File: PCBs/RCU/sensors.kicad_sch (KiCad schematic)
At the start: 8 parts, among them U500 APDS-9306-065, U501 LSM6DS3, U502 SHT30-DIS

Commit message: Schematic cleanup
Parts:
- C504: value 0.1u -> (none)
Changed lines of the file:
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@@
       (effects (font (size 1.27 1.27)) (justify left))
     )
-    (property "Value" "0.1u" (id 1) (at 21.59 113.0299 0)
+    (property "Value" "" (id 1) (at 21.59 113.0299 0)
       (effects (font (size 1.27 1.27)) (justify left))
     )

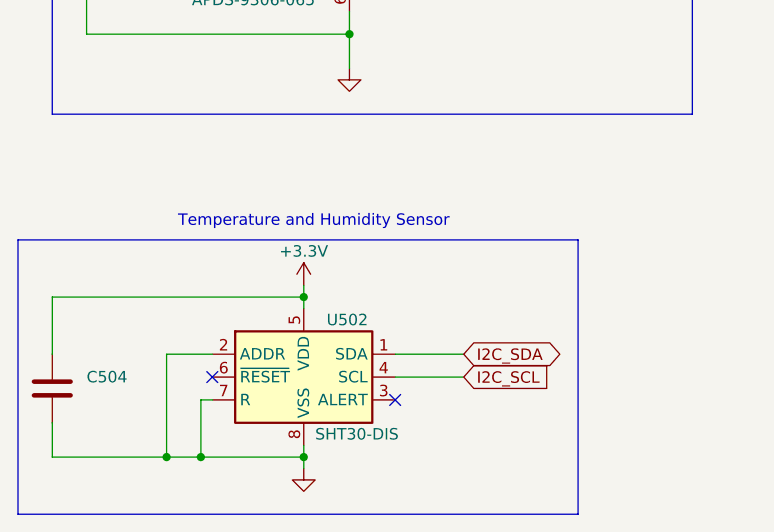
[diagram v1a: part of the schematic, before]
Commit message: Wrote that first regulator in power schematic also powers the external memory
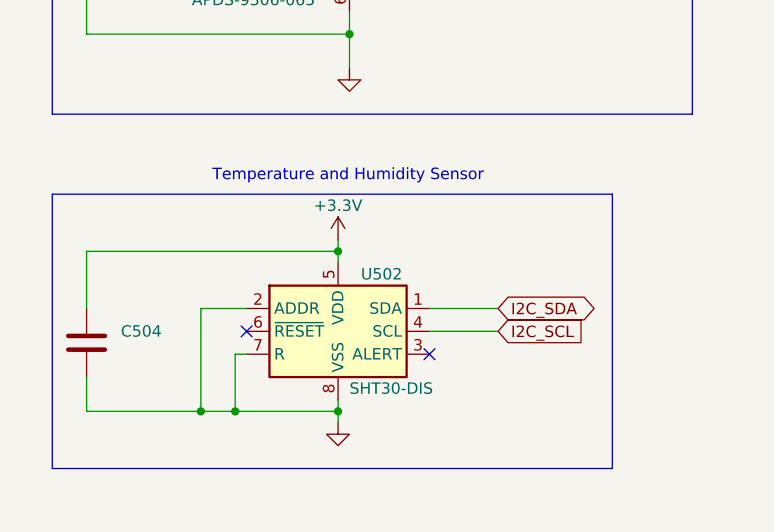
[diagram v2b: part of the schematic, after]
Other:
- moved on the sheet: C504, U502

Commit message: Corrected SPI_MOSI and SPI_MISO labels on U700 - external memory
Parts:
- C504: value (none) -> 0.1uF
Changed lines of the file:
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@@
       (effects (font (size 1.27 1.27)) (justify left))
     )
-    (property "Value" "" (id 1) (at 25.4 107.9499 0)
+    (property "Value" "0.1uF" (id 1) (at 25.4 107.9499 0)
       (effects (font (size 1.27 1.27)) (justify left))
     )

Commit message: Change address pin of left motor ADC to floating so that it and the light sensor will have diffeent addresses, wrote slave addresses for ADCs and light sensor
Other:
- note added: "Slave Address: 1010010"
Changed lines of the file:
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@@
+    (effects (font (size 1.27 1.27)) (justify left bottom))
+  )
+  (text "Slave Address: 1010010" (at 55.88 69.85 0)
     (effects (font (size 1.27 1.27)) (justify left bottom))
   )

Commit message: Wrote slave address for all I2C ICs in binary and hex
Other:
- note added: "Slave Address: 1000100 - 0x44"
- note added: "Slave Address: 1010010 - 0x52"
- note added: "Slave Address: 1101010 - 0x6A"
- note removed: "Slave Address: 1010010"
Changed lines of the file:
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@@
     (stroke (width 0) (type default) (color 0 0 0 0))
   )
-  (polyline (pts (xy 80.01 120.65) (xy 17.78 120.65))
+  (polyline (pts (xy 85.09 120.65) (xy 17.78 120.65))
     (stroke (width 0) (type default) (color 0 0 0 0))
   )
@@
     (stroke (width 0) (type default) (color 0 0 0 0))
   )
-  (polyline (pts (xy 80.01 90.17) (xy 80.01 120.65))
+  (polyline (pts (xy 85.09 90.17) (xy 85.09 120.65))
     (stroke (width 0) (type default) (color 0 0 0 0))
   )
@@
     (stroke (width 0) (type default) (color 0 0 0 0))
   )
-  (polyline (pts (xy 17.78 90.17) (xy 80.01 90.17))
+  (polyline (pts (xy 17.78 90.17) (xy 85.09 90.17))
     (stroke (width 0) (type default) (color 0 0 0 0))
+  )
+  (text "Slave Address: 1101010 - 0x6A" (at 154.94 86.36 0)
+    (effects (font (size 1.27 1.27)) (justify left bottom))
   )
   (text "Temperature and Humidity Sensor" (at 35.56 88.9 0)
@@
     (effects (font (size 5.08 5.08) (thickness 1.016) bold italic) (justify left bottom))
   )
+  (text "Slave Address: 1000100 - 0x44" (at 52.07 115.57 0)
+    (effects (font (size 1.27 1.27)) (justify left bottom))
+  )
   (text "Accelerometer & Gyroscope" (at 129.54 36.83 0)
     (effects (font (size 1.27 1.27)) (justify left bottom))
@@
     (effects (font (size 1.27 1.27)) (justify left bottom))
   )
-  (text "Slave Address: 1010010" (at 55.88 69.85 0)
+  (text "Slave Address: 1010010 - 0x52" (at 55.88 69.85 0)
     (effects (font (size 1.27 1.27)) (justify left bottom))
   )

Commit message: Add footrpints to TVS diodes in [3]
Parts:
- C500: value 1uF -> (none)
- C501, C502, C504: value 0.1uF -> (none)
- R500: value 10k -> (none)
- U500: value APDS-9306-065 -> (none); footprint OptoDevice:Broadcom_DFN-6_2x2mm_P0.65mm -> (none)
- U501: value LSM6DS3 -> (none); footprint Package_LGA:LGA-14_3x2.5mm_P0.5mm_LayoutBorder3x4y -> (none)
- U502: value SHT30-DIS -> (none); footprint Sensor_Humidity:Sensirion_DFN-8-1EP_2.5x2.5mm_P0.5mm_EP1.1x1.7mm -> (none)
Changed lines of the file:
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@@
   (symbol (lib_id "power:GND") (at 120.65 62.23 0) (unit 1)
     (in_bom yes) (on_board yes) (fields_autoplaced)
-    (property "Reference" "#PWR?" (id 0) (at 120.65 68.58 0)
+    (property "Reference" "#PWR0178" (id 0) (at 120.65 68.58 0)
       (effects (font (size 1.27 1.27)) hide)
     )
@@
   (symbol (lib_id "power:GND") (at 161.29 67.31 0) (unit 1)
     (in_bom yes) (on_board yes) (fields_autoplaced)
-    (property "Reference" "#PWR?" (id 0) (at 161.29 73.66 0)
+    (property "Reference" "#PWR0184" (id 0) (at 161.29 73.66 0)
       (effects (font (size 1.27 1.27)) hide)
     )
@@
       (effects (font (size 1.27 1.27)) (justify left))
     )
-    (property "Value" "1uF" (id 1) (at 25.4 63.4999 0)
+    (property "Value" "" (id 1) (at 25.4 63.4999 0)
       (effects (font (size 1.27 1.27)) (justify left))
     )
@@
   (symbol (lib_id "power:GND") (at 50.8 76.2 0) (unit 1)
     (in_bom yes) (on_board yes) (fields_autoplaced)
-    (property "Reference" "#PWR?" (id 0) (at 50.8 82.55 0)
+    (property "Reference" "#PWR0182" (id 0) (at 50.8 82.55 0)
       (effects (font (size 1.27 1.27)) hide)
     )
@@
   (symbol (lib_id "power:+3.3V") (at 50.8 50.8 0) (unit 1)
     (in_bom yes) (on_board yes)
-    (property "Reference" "#PWR?" (id 0) (at 50.8 54.61 0)
+    (property "Reference" "#PWR0181" (id 0) (at 50.8 54.61 0)
       (effects (font (size 1.27 1.27)) hide)
     )
@@
   (symbol (lib_id "power:+3.3V") (at 119.38 92.71 0) (unit 1)
     (in_bom yes) (on_board yes)
-    (property "Reference" "#PWR?" (id 0) (at 119.38 96.52 0)
+    (property "Reference" "#PWR0179" (id 0) (at 119.38 96.52 0)
       (effects (font (size 1.27 1.27)) hide)
     )
@@
       (effects (font (size 1.27 1.27)) (justify left))
     )
-    (property "Value" "SHT30-DIS" (id 1) (at 50.8 111.76 0)
-      (effects (font (size 1.27 1.27)) (justify left))
-    )
-    (property "Footprint" "Sensor_Humidity:Sensirion_DFN-8-1EP_2.5x2.5mm_P0.5mm_EP1.1x1.7mm" (id 2) (at 49.53 104.14 0)
+    (property "Value" "" (id 1) (at 50.8 111.76 0)
+      (effects (font (size 1.27 1.27)) (justify left))
+    )
+    (property "Footprint" "" (id 2) (at 49.53 104.14 0)
       (effects (font (size 1.27 1.27)) hide)
     )
@@
   (symbol (lib_id "power:+3.3V") (at 142.24 44.45 0) (unit 1)
     (in_bom yes) (on_board yes)
-    (property "Reference" "#PWR?" (id 0) (at 142.24 48.26 0)
+    (property "Reference" "#PWR0183" (id 0) (at 142.24 48.26 0)
       (effects (font (size 1.27 1.27)) hide)
     )
@@
   (symbol (lib_id "power:GND") (at 49.53 115.57 0) (unit 1)
     (in_bom yes) (on_board yes) (fields_autoplaced)
-    (property "Reference" "#PWR?" (id 0) (at 49.53 121.92 0)
+    (property "Reference" "#PWR0176" (id 0) (at 49.53 121.92 0)
       (effects (font (size 1.27 1.27)) hide)
     )
@@
       (effects (font (size 1.27 1.27)) (justify left))
     )
-    (property "Value" "10k" (id 1) (at 82.55 62.23 0)
+    (property "Value" "" (id 1) (at 82.55 62.23 0)
       (effects (font (size 1.27 1.27)) (justify left))
     )
@@
       (effects (font (size 1.27 1.27)) (justify right))
     )
-    (property "Value" "APDS-9306-065" (id 1) (at 46.99 68.58 0)
-      (effects (font (size 1.27 1.27)) (justify right))
-    )
-    (property "Footprint" "OptoDevice:Broadcom_DFN-6_2x2mm_P0.65mm" (id 2) (at 48.26 74.93 0)
+    (property "Value" "" (id 1) (at 46.99 68.58 0)
+      (effects (font (size 1.27 1.27)) (justify right))
+    )
+    (property "Footprint" "" (id 2) (at 48.26 74.93 0)
       (effects (font (size 1.27 1.27)) hide)
     )
@@
       (effects (font (size 1.27 1.27)) (justify left))
     )
-    (property "Value" "0.1uF" (id 1) (at 25.4 107.9499 0)
+    (property "Value" "" (id 1) (at 25.4 107.9499 0)
       (effects (font (size 1.27 1.27)) (justify left))
     )
@@
       (effects (font (size 1.27 1.27)) (justify right))
     )
-    (property "Value" "0.1uF" (id 1) (at 162.56 64.77 0)
+    (property "Value" "" (id 1) (at 162.56 64.77 0)
       (effects (font (size 1.27 1.27)) (justify right))
     )
@@
   (symbol (lib_id "power:+3.3V") (at 49.53 95.25 0) (unit 1)
     (in_bom yes) (on_board yes)
-    (property "Reference" "#PWR?" (id 0) (at 49.53 99.06 0)
+    (property "Reference" "#PWR0177" (id 0) (at 49.53 99.06 0)
       (effects (font (size 1.27 1.27)) hide)
     )
@@
   (symbol (lib_id "power:GND") (at 104.14 78.74 0) (unit 1)
     (in_bom yes) (on_board yes) (fields_autoplaced)
-    (property "Reference" "#PWR?" (id 0) (at 104.14 85.09 0)
+    (property "Reference" "#PWR0180" (id 0) (at 104.14 85.09 0)
       (effects (font (size 1.27 1.27)) hide)
     )
@@
     (in_bom yes) (on_board yes)
     (property "Reference" "U501" (id 0) (at 149.86 64.77 0))
-    (property "Value" "LSM6DS3" (id 1) (at 148.59 90.17 0))
-    (property "Footprint" "Package_LGA:LGA-14_3x2.5mm_P0.5mm_LayoutBorder3x4y" (id 2) (at 130.81 95.25 0)
+    (property "Value" "" (id 1) (at 148.59 90.17 0))
+    (property "Footprint" "" (id 2) (at 130.81 95.25 0)
       (effects (font (size 1.27 1.27)) (justify left) hide)
     )
@@
       (effects (font (size 1.27 1.27)) (justify left))
     )
-    (property "Value" "0.1uF" (id 1) (at 127 59.69 0)
+    (property "Value" "" (id 1) (at 127 59.69 0)
       (effects (font (size 1.27 1.27)) (justify left))
     )
@@
   (symbol (lib_id "power:GND") (at 143.51 96.52 0) (unit 1)
     (in_bom yes) (on_board yes) (fields_autoplaced)
-    (property "Reference" "#PWR?" (id 0) (at 143.51 102.87 0)
-      (effects (font (size 1.27 1.27)) hide)
-    )
+    (property "Reference" "#PWR0185" (id 0) (at 143.51 102.87 0)
+      (effects (font (size 1.27 1.27)) hide)
+    )

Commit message: Passed ERC
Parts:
- C500: value (none) -> 1uF; footprint (none) -> Capacitor_SMD:C_0603_1608Metric
- C501, C502, C504: value (none) -> 0.1uF; footprint (none) -> Capacitor_SMD:C_0603_1608Metric
- R500: value (none) -> 10k; footprint (none) -> Resistor_SMD:R_0603_1608Metric
- U500: value (none) -> APDS-9306-065; footprint (none) -> OptoDevice:Broadcom_DFN-6_2x2mm_P0.65mm
- U501: value (none) -> LSM6DS3; footprint (none) -> Package_LGA:LGA-14_3x2.5mm_P0.5mm_LayoutBorder3x4y
- U502: value (none) -> SHT30-DIS; footprint (none) -> Sensor_Humidity:Sensirion_DFN-8-1EP_2.5x2.5mm_P0.5mm_EP1.1x1.7mm
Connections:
- no-connect marks 4 -> 5
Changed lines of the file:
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@@
   (no_connect (at 156.21 69.85))
   (no_connect (at 59.69 107.95))
+  (no_connect (at 140.97 92.71))
   (no_connect (at 39.37 105.41))
   (wire (pts (xy 104.14 72.39) (xy 125.73 72.39))
@@
       (effects (font (size 1.27 1.27)) (justify left))
     )
-    (property "Value" "" (id 1) (at 25.4 63.4999 0)
-      (effects (font (size 1.27 1.27)) (justify left))
-    )
-    (property "Footprint" "" (id 2) (at 22.5552 66.04 0)
+    (property "Value" "1uF" (id 1) (at 25.4 63.4999 0)
+      (effects (font (size 1.27 1.27)) (justify left))
+    )
+    (property "Footprint" "Capacitor_SMD:C_0603_1608Metric" (id 2) (at 22.5552 66.04 0)
       (effects (font (size 1.27 1.27)) hide)
     )
@@
       (effects (font (size 1.27 1.27)) (justify left))
     )
-    (property "Value" "" (id 1) (at 50.8 111.76 0)
-      (effects (font (size 1.27 1.27)) (justify left))
-    )
-    (property "Footprint" "" (id 2) (at 49.53 104.14 0)
+    (property "Value" "SHT30-DIS" (id 1) (at 50.8 111.76 0)
+      (effects (font (size 1.27 1.27)) (justify left))
+    )
+    (property "Footprint" "Sensor_Humidity:Sensirion_DFN-8-1EP_2.5x2.5mm_P0.5mm_EP1.1x1.7mm" (id 2) (at 49.53 104.14 0)
       (effects (font (size 1.27 1.27)) hide)
     )
@@
       (effects (font (size 1.27 1.27)) (justify left))
     )
-    (property "Value" "" (id 1) (at 82.55 62.23 0)
-      (effects (font (size 1.27 1.27)) (justify left))
-    )
-    (property "Footprint" "" (id 2) (at 79.502 60.96 90)
+    (property "Value" "10k" (id 1) (at 82.55 62.23 0)
+      (effects (font (size 1.27 1.27)) (justify left))
+    )
+    (property "Footprint" "Resistor_SMD:R_0603_1608Metric" (id 2) (at 79.502 60.96 90)
       (effects (font (size 1.27 1.27)) hide)
     )
@@
       (effects (font (size 1.27 1.27)) (justify right))
     )
-    (property "Value" "" (id 1) (at 46.99 68.58 0)
+    (property "Value" "APDS-9306-065" (id 1) (at 46.99 68.58 0)
       (effects (font (size 1.27 1.27)) (justify right))
     )
-    (property "Footprint" "" (id 2) (at 48.26 74.93 0)
+    (property "Footprint" "OptoDevice:Broadcom_DFN-6_2x2mm_P0.65mm" (id 2) (at 48.26 74.93 0)
       (effects (font (size 1.27 1.27)) hide)
     )
@@
       (effects (font (size 1.27 1.27)) (justify left))
     )
-    (property "Value" "" (id 1) (at 25.4 107.9499 0)
-      (effects (font (size 1.27 1.27)) (justify left))
-    )
-    (property "Footprint" "" (id 2) (at 22.5552 110.49 0)
+    (property "Value" "0.1uF" (id 1) (at 25.4 107.9499 0)
+      (effects (font (size 1.27 1.27)) (justify left))
+    )
+    (property "Footprint" "Capacitor_SMD:C_0603_1608Metric" (id 2) (at 22.5552 110.49 0)
       (effects (font (size 1.27 1.27)) hide)
     )
@@
       (effects (font (size 1.27 1.27)) (justify right))
     )
-    (property "Value" "" (id 1) (at 162.56 64.77 0)
+    (property "Value" "0.1uF" (id 1) (at 162.56 64.77 0)
       (effects (font (size 1.27 1.27)) (justify right))
     )
-    (property "Footprint" "" (id 2) (at 160.3248 58.42 0)
+    (property "Footprint" "Capacitor_SMD:C_0603_1608Metric" (id 2) (at 160.3248 58.42 0)
       (effects (font (size 1.27 1.27)) hide)
     )
@@
     (in_bom yes) (on_board yes)
     (property "Reference" "U501" (id 0) (at 149.86 64.77 0))
-    (property "Value" "" (id 1) (at 148.59 90.17 0))
-    (property "Footprint" "" (id 2) (at 130.81 95.25 0)
+    (property "Value" "LSM6DS3" (id 1) (at 148.59 90.17 0))
+    (property "Footprint" "Package_LGA:LGA-14_3x2.5mm_P0.5mm_LayoutBorder3x4y" (id 2) (at 130.81 95.25 0)
       (effects (font (size 1.27 1.27)) (justify left) hide)
     )
@@
       (effects (font (size 1.27 1.27)) (justify left))
     )
-    (property "Value" "" (id 1) (at 127 59.69 0)
-      (effects (font (size 1.27 1.27)) (justify left))
-    )
-    (property "Footprint" "" (id 2) (at 119.6848 53.34 0)
-      (effects (font (size 1.27 1.27)) hide)
-    )
+    (property "Value" "0.1uF" (id 1) (at 127 59.69 0)
+      (effects (font (size 1.27 1.27)) (justify left))
+    )
+    (property "Footprint" "Capacitor_SMD:C_0603_1608Metric" (id 2) (at 119.6848 53.34 0)
+      (effects (font (size 1.27 1.27)) hide)
+    )

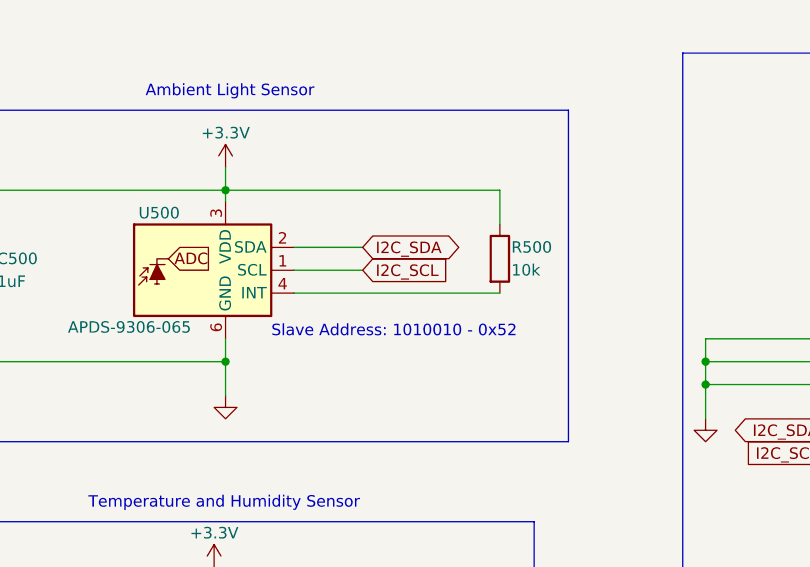
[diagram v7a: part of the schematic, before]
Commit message: USB2 can now power all modules except motor control if it is the only power source that is plugged in
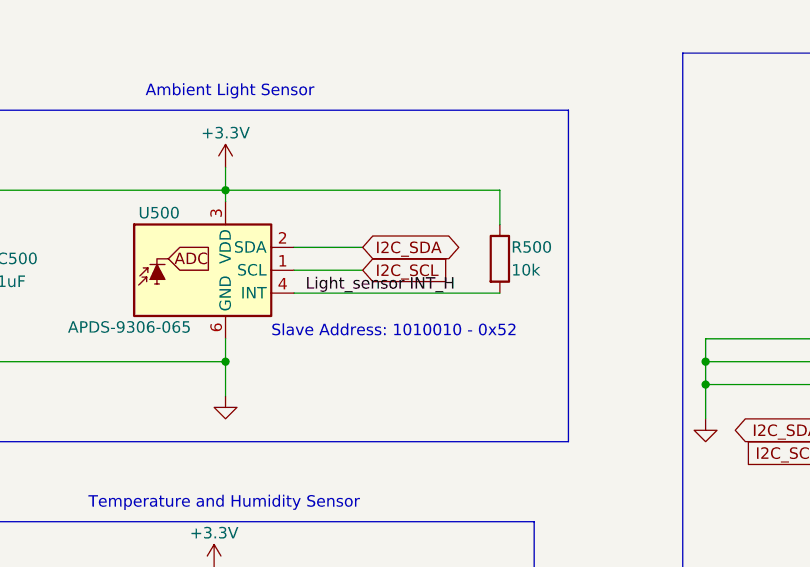
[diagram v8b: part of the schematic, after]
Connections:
- net Light_sensor INT_H: now reaches R500.2, U500.4 (INT)
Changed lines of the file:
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@@
+    (effects (font (size 1.27 1.27)) (justify left bottom))
+  )
+  (label "Light_sensor INT_H" (at 59.69 64.77 0)
     (effects (font (size 1.27 1.27)) (justify left bottom))
   )
